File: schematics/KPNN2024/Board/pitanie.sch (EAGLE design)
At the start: 46 parts, among them X1 PERE, X2 AKKUM

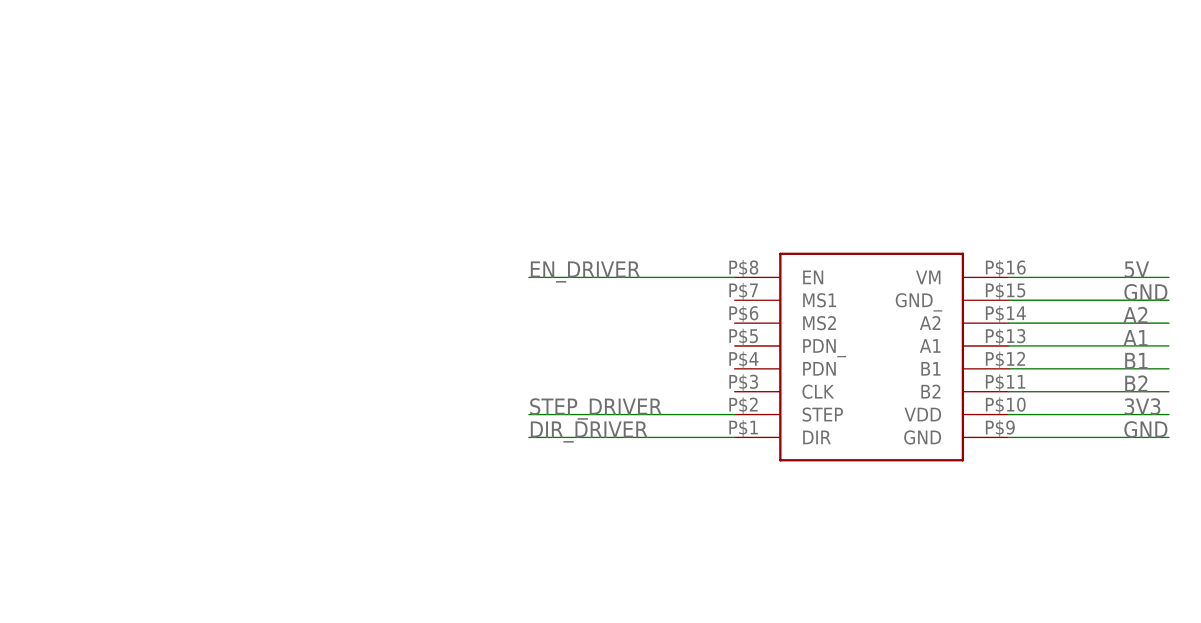
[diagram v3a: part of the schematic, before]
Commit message: поправила платы
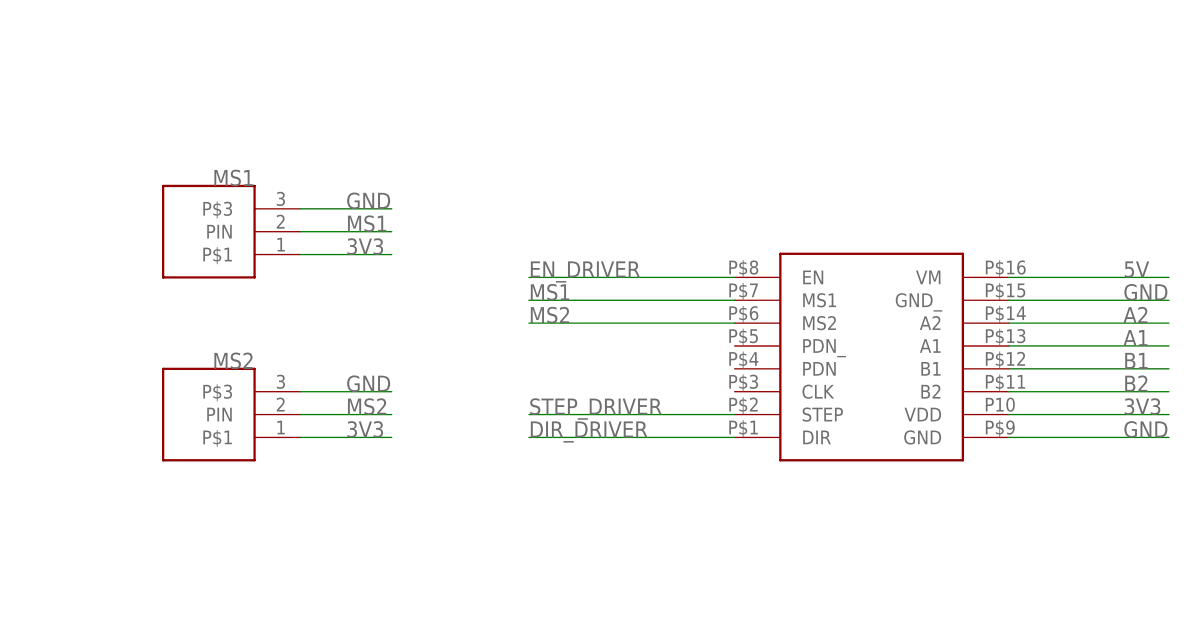
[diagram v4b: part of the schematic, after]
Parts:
- added MS1, MS2: CONNECT_3, UNKNOWN-2024:CONNECT_3
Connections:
- new net MS1: DRIVER.MS1, MS1.PIN
- new net MS2: DRIVER.MS2, MS2.PIN
- net 3V3: now also MS1.P$1, MS2.P$1
- net GND: now also MS1.P$3, MS2.P$3

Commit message: Модели поправлены в соответствии с платами
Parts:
- added U$1: Плата питания, UNKNOWN-2024:LOGOPCB-""
- R2, R5: value 8k87 -> 10k
- R3: value 40k2 -> 31k6
- R6: value 40k2 -> 53k6
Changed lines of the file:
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@@
 <part name="C3" library="rcl" library_urn="urn:adsk.eagle:library:334" deviceset="C-US" device="C0603" package3d_urn="urn:adsk.eagle:package:23616/2" value="22u"/>
 <part name="C4" library="rcl" library_urn="urn:adsk.eagle:library:334" deviceset="C-US" device="C0603" package3d_urn="urn:adsk.eagle:package:23616/2" value="0,1u"/>
-<part name="R2" library="rcl" library_urn="urn:adsk.eagle:library:334" deviceset="R-US_" device="R0603" package3d_urn="urn:adsk.eagle:package:23555/3" value="8k87"/>
-<part name="R3" library="rcl" library_urn="urn:adsk.eagle:library:334" deviceset="R-US_" device="R0603" package3d_urn="urn:adsk.eagle:package:23555/3" value="40k2"/>
+<part name="R2" library="rcl" library_urn="urn:adsk.eagle:library:334" deviceset="R-US_" device="R0603" package3d_urn="urn:adsk.eagle:package:23555/3" value="10k"/>
+<part name="R3" library="rcl" library_urn="urn:adsk.eagle:library:334" deviceset="R-US_" device="R0603" package3d_urn="urn:adsk.eagle:package:23555/3" value="31k6"/>
 <part name="C5" library="rcl" library_urn="urn:adsk.eagle:library:334" deviceset="C-US" device="C0603" package3d_urn="urn:adsk.eagle:package:23616/2" value="33p"/>
 <part name="C6" library="rcl" library_urn="urn:adsk.eagle:library:334" deviceset="C-US" device="C1206" package3d_urn="urn:adsk.eagle:package:23618/2" value="22u"/>
@@
 <part name="C10" library="rcl" library_urn="urn:adsk.eagle:library:334" deviceset="C-US" device="C0603" package3d_urn="urn:adsk.eagle:package:23616/2" value="22u"/>
 <part name="C11" library="rcl" library_urn="urn:adsk.eagle:library:334" deviceset="C-US" device="C0603" package3d_urn="urn:adsk.eagle:package:23616/2" value="0,1u"/>
-<part name="R5" library="rcl" library_urn="urn:adsk.eagle:library:334" deviceset="R-US_" device="R0603" package3d_urn="urn:adsk.eagle:package:23555/3" value="8k87"/>
-<part name="R6" library="rcl" library_urn="urn:adsk.eagle:library:334" deviceset="R-US_" device="R0603" package3d_urn="urn:adsk.eagle:package:23555/3" value="40k2"/>
+<part name="R5" library="rcl" library_urn="urn:adsk.eagle:library:334" deviceset="R-US_" device="R0603" package3d_urn="urn:adsk.eagle:package:23555/3" value="10k"/>
+<part name="R6" library="rcl" library_urn="urn:adsk.eagle:library:334" deviceset="R-US_" device="R0603" package3d_urn="urn:adsk.eagle:package:23555/3" value="53k6"/>
 <part name="C12" library="rcl" library_urn="urn:adsk.eagle:library:334" deviceset="C-US" device="C0603" package3d_urn="urn:adsk.eagle:package:23616/2" value="33p"/>
 <part name="C13" library="rcl" library_urn="urn:adsk.eagle:library:334" deviceset="C-US" device="C1206" package3d_urn="urn:adsk.eagle:package:23618/2" value="22u"/>
@@
 <part name="MS1" library="UNKNOWN-2024" deviceset="CONNECT_3" device=""/>
 <part name="MS2" library="UNKNOWN-2024" deviceset="CONNECT_3" device=""/>
+<part name="U$1" library="UNKNOWN-2024" deviceset="LOGO" device="PCB-&quot;&quot;" value="Плата питания"/>
 </parts>
 <sheets>
@@
 <attribute name="NAME" x="312.42" y="86.36" size="1.778" layer="95" rot="MR0"/>
 </instance>
+<instance part="U$1" gate="G$1" x="154.94" y="210.82" smashed="yes">
+<attribute name="VALUE" x="259.08" y="210.82" size="12.7" layer="96"/>
+</instance>
 </instances>
